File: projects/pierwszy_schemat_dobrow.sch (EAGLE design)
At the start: 36 parts, among them IC1 74HC595N, IC2 7805T, IC3 LD117AV, U2 ARDUINOR3-DIMENSION

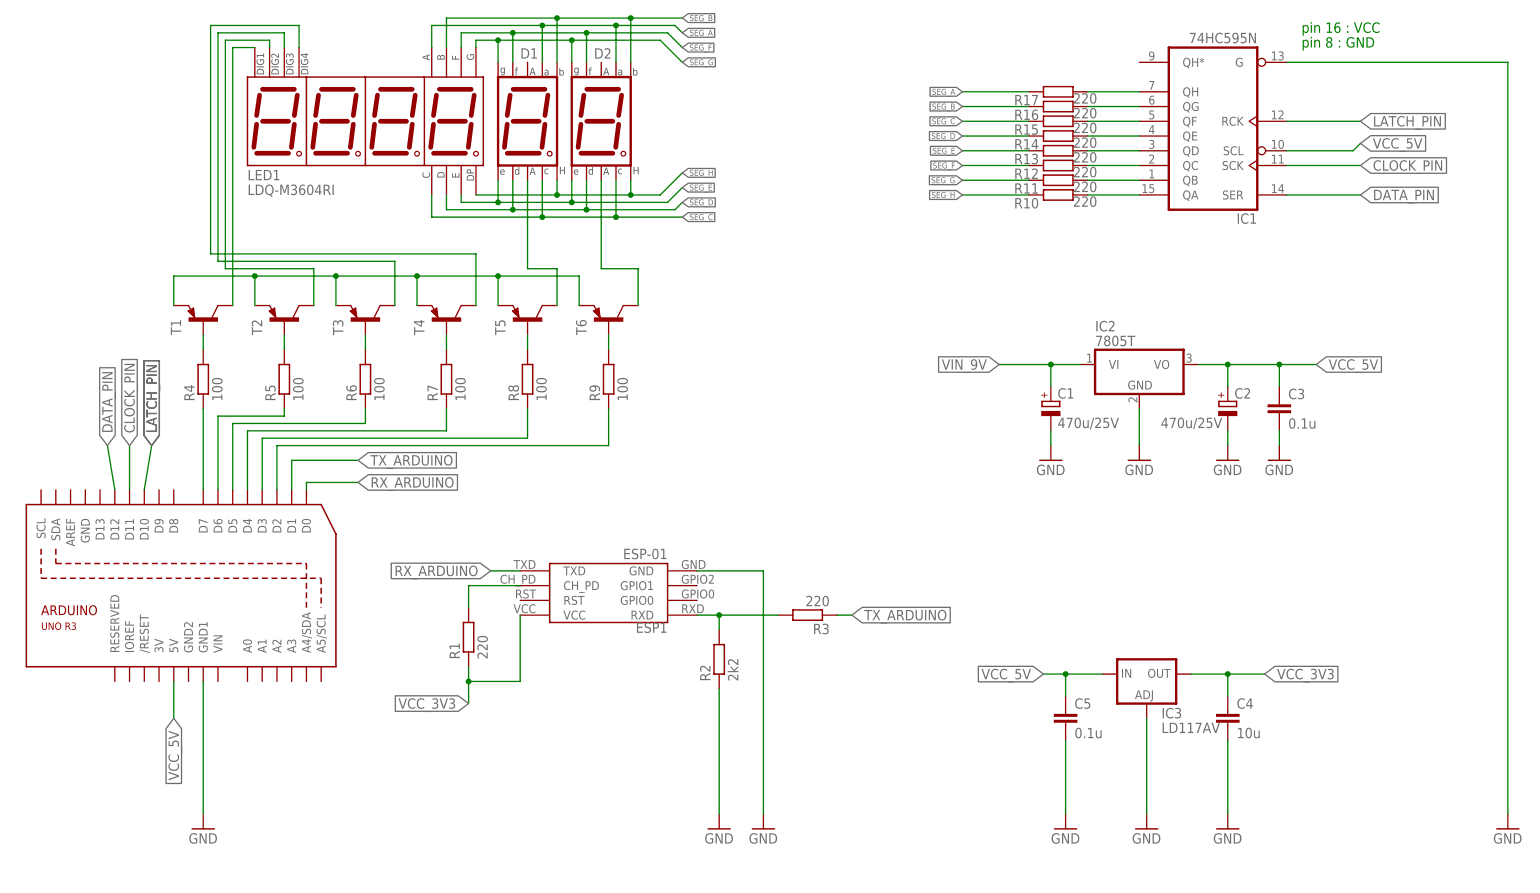
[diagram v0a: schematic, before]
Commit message: changed arduino to pro mini
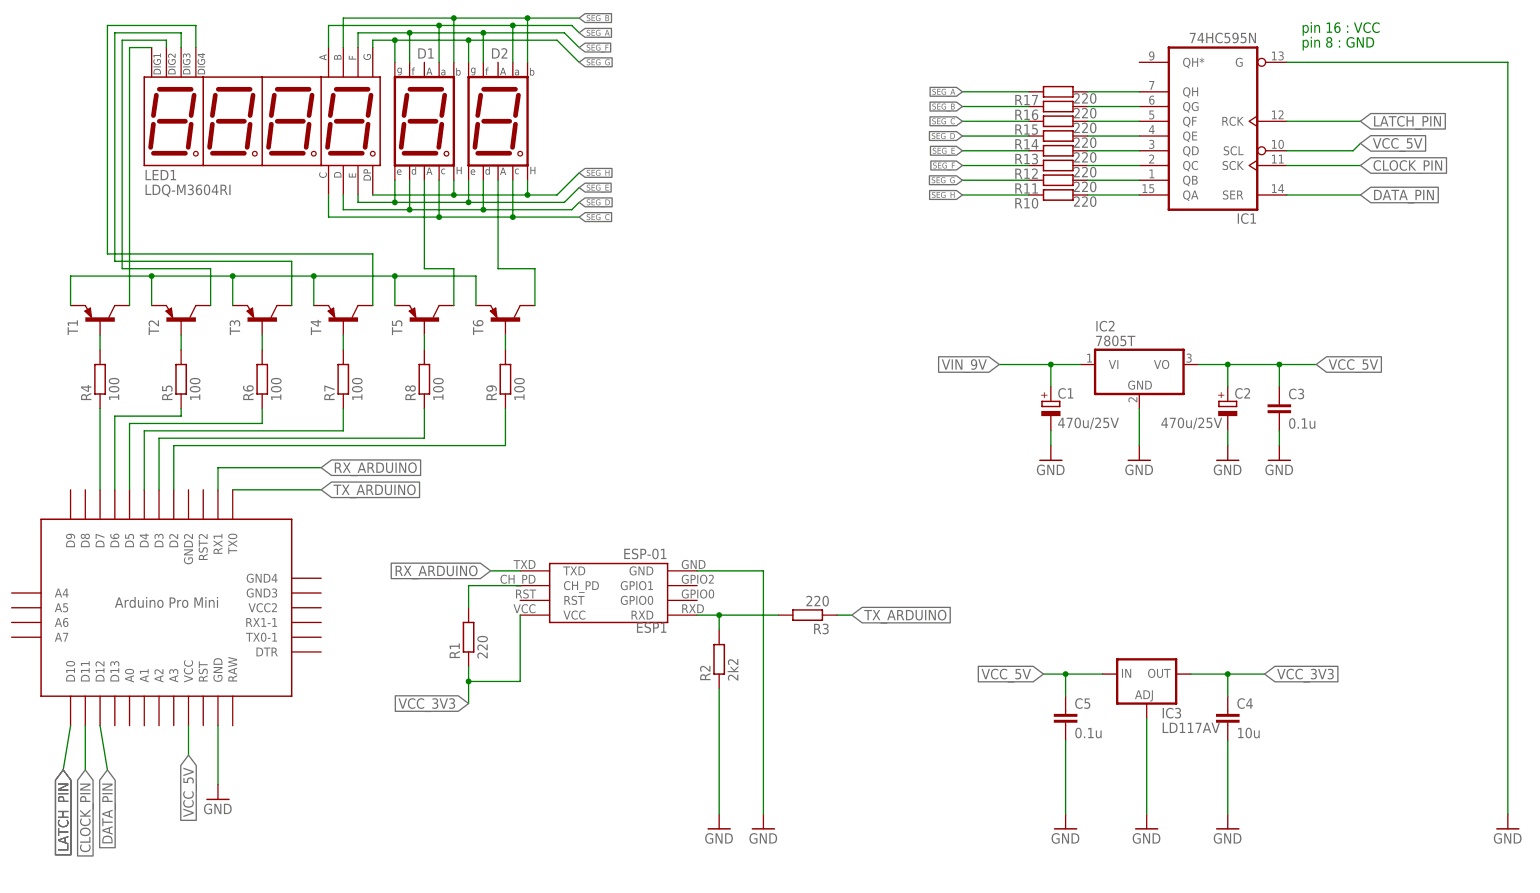
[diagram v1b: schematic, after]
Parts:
- removed U2: ARDUINOR3-DIMENSION, arduino_UNO_edit:ARDUINOR3-DIMENSION
- added U$1: PRO-MINI, Arduino-clone:PRO-MINI
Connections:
- removed net N$20: U2.GND1
- net CLOCK_PIN: now also U$1.D11; no longer U2.D11
- net DATA_PIN: now also U$1.D12; no longer U2.D12
- net GND: now also U$1.GND
- net LATCH_PIN: now also U$1.D10; no longer U2.D10
- net N$31: now also U$1.D7; no longer U2.D7
- net N$32: now also U$1.D6; no longer U2.D6
- net N$33: now also U$1.D5; no longer U2.D5
- net N$34: now also U$1.D4; no longer U2.D4
- net N$35: now also U$1.D3; no longer U2.D3
- net N$36: now also U$1.D2; no longer U2.D2
- net RX_ARDUINO: now also U$1.RX1; no longer U2.D0
- net TX_ARDUINO: now also U$1.TX0; no longer U2.D1
- net VCC_5V: now also U$1.VCC; no longer U2.5V
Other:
- moved on the sheet: D1, D2, LED1, R4, R5, R6, R7, R8, R9, T1, T2, T3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

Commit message: repaired gnd connection
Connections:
- removed net N$21: C2.-
- net GND: now also C2.-
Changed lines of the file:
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@@
 <setting verticaltext="up"/>
 </settings>
-<grid distance="1.27" unitdist="mm" unit="mm" style="lines" multiple="1" display="yes" altdistance="0.01" altunitdist="inch" altunit="inch"/>
+<grid distance="0.1" unitdist="inch" unit="inch" style="lines" multiple="1" display="no" altdistance="0.01" altunitdist="inch" altunit="inch"/>
 <layers>
 <layer number="1" name="Top" color="4" fill="1" visible="no" active="no"/>
@@
 <part name="C3" library="rcl" library_urn="urn:adsk.eagle:library:334" deviceset="C-EU" device="025-025X050" package3d_urn="urn:adsk.eagle:package:23629/2" value="0.1u"/>
 <part name="GND2" library="supply1" library_urn="urn:adsk.eagle:library:371" deviceset="GND" device=""/>
-<part name="GND6" library="supply1" library_urn="urn:adsk.eagle:library:371" deviceset="GND" device=""/>
 <part name="GND7" library="supply1" library_urn="urn:adsk.eagle:library:371" deviceset="GND" device=""/>
 <part name="IC3" library="v-reg" library_urn="urn:adsk.eagle:library:409" deviceset="LD117A?*" device="V" package3d_urn="urn:adsk.eagle:package:30365/1"/>
@@
 <part name="FRAME1" library="frames" library_urn="urn:adsk.eagle:library:229" deviceset="DOCFIELD" device=""/>
 <part name="U$1" library="Arduino-clone" deviceset="PRO-MINI" device=""/>
+<part name="GND6" library="supply1" library_urn="urn:adsk.eagle:library:371" deviceset="GND" device=""/>
 </parts>
 <sheets>
@@
 <attribute name="VALUE" x="185.42" y="106.68" size="1.778" layer="96"/>
 </instance>
-<instance part="GND6" gate="1" x="218.44" y="109.22" smashed="yes">
-<attribute name="VALUE" x="215.9" y="106.68" size="1.778" layer="96"/>
-</instance>
 <instance part="GND7" gate="1" x="227.33" y="109.22" smashed="yes">
 <attribute name="VALUE" x="224.79" y="106.68" size="1.778" layer="96"/>
@@
 </instance>
 <instance part="U$1" gate="G$1" x="26.67" y="81.28" smashed="yes" rot="R270"/>
+<instance part="GND6" gate="1" x="218.44" y="109.22" smashed="yes">
+<attribute name="VALUE" x="215.9" y="106.68" size="1.778" layer="96"/>
+</instance>
 </instances>
 <busses>
@@
 <wire x1="44.45" y1="53.34" x2="44.45" y2="63.5" width="0.1524" layer="91"/>
 </segment>
+<segment>
+<pinref part="C2" gate="G$1" pin="-"/>
+<wire x1="218.44" y1="114.3" x2="218.44" y2="111.76" width="0.1524" layer="91"/>
+<pinref part="GND6" gate="1" pin="GND"/>
+</segment>
 </net>
 <net name="TX_ARDUINO" class="0">
@@
 </segment>
 </net>
-<net name="N$21" class="0">
-<segment>
-<pinref part="C2" gate="G$1" pin="-"/>
-<wire x1="218.44" y1="114.3" x2="218.44" y2="111.76" width="0.1524" layer="91"/>
-<pinref part="GND6" gate="1" pin="GND"/>
-</segment>
-</net>

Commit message: repair v2
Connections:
- removed net N$11: C1.-
- net GND: now also C1.-
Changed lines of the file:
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@@
 <part name="C2" library="rcl" library_urn="urn:adsk.eagle:library:334" deviceset="CPOL-EU" device="E5-8.5" package3d_urn="urn:adsk.eagle:package:23374/1" value="470u/25V"/>
 <part name="C3" library="rcl" library_urn="urn:adsk.eagle:library:334" deviceset="C-EU" device="025-025X050" package3d_urn="urn:adsk.eagle:package:23629/2" value="0.1u"/>
-<part name="GND2" library="supply1" library_urn="urn:adsk.eagle:library:371" deviceset="GND" device=""/>
 <part name="GND7" library="supply1" library_urn="urn:adsk.eagle:library:371" deviceset="GND" device=""/>
 <part name="IC3" library="v-reg" library_urn="urn:adsk.eagle:library:409" deviceset="LD117A?*" device="V" package3d_urn="urn:adsk.eagle:package:30365/1"/>
@@
 <part name="U$1" library="Arduino-clone" deviceset="PRO-MINI" device=""/>
 <part name="GND6" library="supply1" library_urn="urn:adsk.eagle:library:371" deviceset="GND" device=""/>
+<part name="GND2" library="supply1" library_urn="urn:adsk.eagle:library:371" deviceset="GND" device=""/>
 </parts>
 <sheets>
@@
 <attribute name="VALUE" x="228.854" y="114.681" size="1.778" layer="96"/>
 </instance>
-<instance part="GND2" gate="1" x="187.96" y="109.22" smashed="yes">
-<attribute name="VALUE" x="185.42" y="106.68" size="1.778" layer="96"/>
-</instance>
 <instance part="GND7" gate="1" x="227.33" y="109.22" smashed="yes">
 <attribute name="VALUE" x="224.79" y="106.68" size="1.778" layer="96"/>
@@
 <instance part="GND6" gate="1" x="218.44" y="109.22" smashed="yes">
 <attribute name="VALUE" x="215.9" y="106.68" size="1.778" layer="96"/>
+</instance>
+<instance part="GND2" gate="1" x="187.96" y="109.22" smashed="yes">
+<attribute name="VALUE" x="185.42" y="106.68" size="1.778" layer="96"/>
 </instance>
 </instances>
@@
 <pinref part="GND6" gate="1" pin="GND"/>
 </segment>
+<segment>
+<pinref part="C1" gate="G$1" pin="-"/>
+<wire x1="187.96" y1="114.3" x2="187.96" y2="111.76" width="0.1524" layer="91"/>
+<pinref part="GND2" gate="1" pin="GND"/>
+</segment>
 </net>
 <net name="TX_ARDUINO" class="0">
@@
 </segment>
 </net>
-<net name="N$11" class="0">
-<segment>
-<pinref part="C1" gate="G$1" pin="-"/>
-<wire x1="187.96" y1="114.3" x2="187.96" y2="111.76" width="0.1524" layer="91"/>
-<pinref part="GND2" gate="1" pin="GND"/>
-</segment>
-</net>

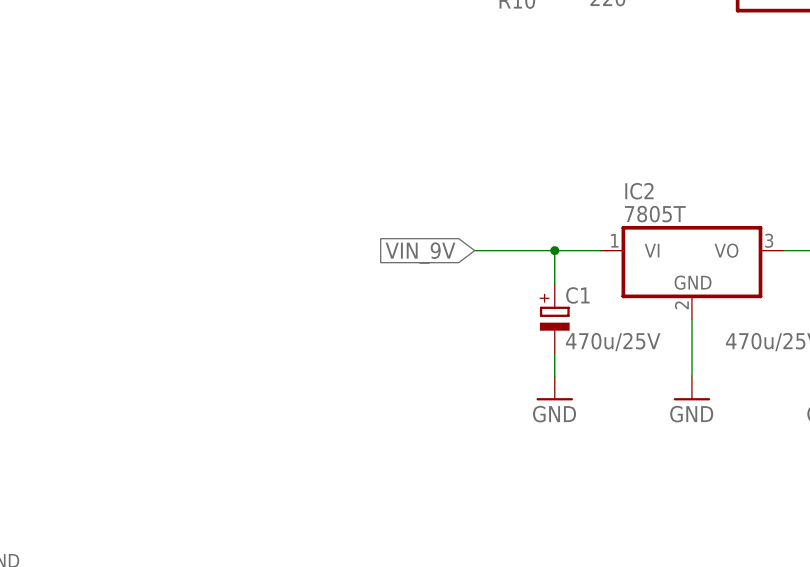
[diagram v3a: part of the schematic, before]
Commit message: Added power jack
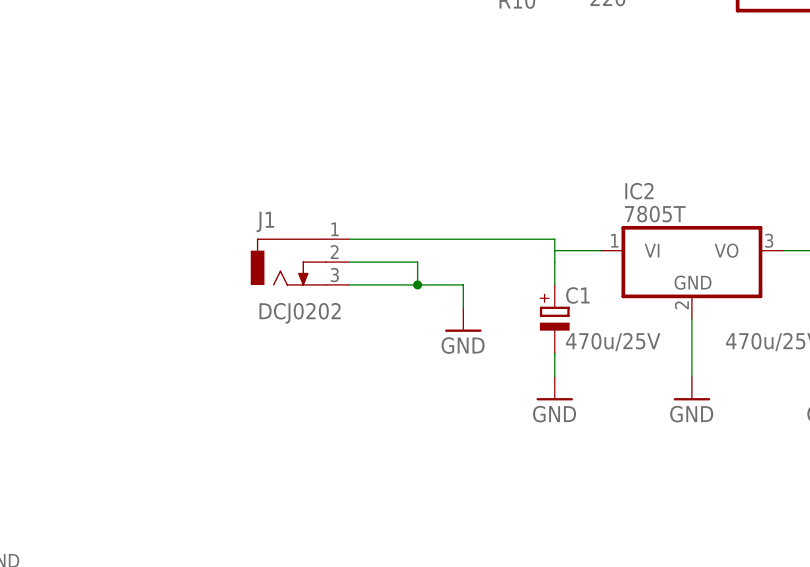
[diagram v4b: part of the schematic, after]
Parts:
- added J1: DCJ0202, con-jack:DCJ0202
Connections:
- net GND: now also J1.2, J1.3
- net VIN_9V: now also J1.1
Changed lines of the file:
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@@
 <layers>
 <layer number="1" name="Top" color="4" fill="1" visible="no" active="no"/>
+<layer number="2" name="Route2" color="1" fill="3" visible="no" active="no"/>
+<layer number="3" name="Route3" color="4" fill="3" visible="no" active="no"/>
+<layer number="4" name="Route4" color="1" fill="4" visible="no" active="no"/>
+<layer number="5" name="Route5" color="4" fill="4" visible="no" active="no"/>
+<layer number="6" name="Route6" color="1" fill="8" visible="no" active="no"/>
+<layer number="7" name="Route7" color="4" fill="8" visible="no" active="no"/>
+<layer number="8" name="Route8" color="1" fill="2" visible="no" active="no"/>
+<layer number="9" name="Route9" color="4" fill="2" visible="no" active="no"/>
+<layer number="10" name="Route10" color="1" fill="7" visible="no" active="no"/>
+<layer number="11" name="Route11" color="4" fill="7" visible="no" active="no"/>
+<layer number="12" name="Route12" color="1" fill="5" visible="no" active="no"/>
+<layer number="13" name="Route13" color="4" fill="5" visible="no" active="no"/>
+<layer number="14" name="Route14" color="1" fill="6" visible="no" active="no"/>
+<layer number="15" name="Route15" color="4" fill="6" visible="no" active="no"/>
 <layer number="16" name="Bottom" color="1" fill="1" visible="no" active="no"/>
 <layer number="17" name="Pads" color="2" fill="1" visible="no" active="no"/>
@@
 <part name="GND6" library="supply1" library_urn="urn:adsk.eagle:library:371" deviceset="GND" device=""/>
 <part name="GND2" library="supply1" library_urn="urn:adsk.eagle:library:371" deviceset="GND" device=""/>
+<part name="J1" library="con-jack" library_urn="urn:adsk.eagle:library:154" deviceset="DCJ0202" device="" package3d_urn="urn:adsk.eagle:package:7491/1"/>
+<part name="GND12" library="supply1" library_urn="urn:adsk.eagle:library:371" deviceset="GND" device=""/>
 </parts>
 <sheets>
@@
 <instance part="GND2" gate="1" x="187.96" y="109.22" smashed="yes">
 <attribute name="VALUE" x="185.42" y="106.68" size="1.778" layer="96"/>
+</instance>
+<instance part="J1" gate="G$1" x="157.48" y="124.46" smashed="yes">
+<attribute name="NAME" x="154.94" y="128.27" size="1.778" layer="95"/>
+<attribute name="VALUE" x="154.94" y="118.11" size="1.778" layer="96"/>
+</instance>
+<instance part="GND12" gate="1" x="177.8" y="116.84" smashed="yes">
+<attribute name="VALUE" x="175.26" y="114.3" size="1.778" layer="96"/>
 </instance>
 </instances>
@@
 <pinref part="GND2" gate="1" pin="GND"/>
 </segment>
+<segment>
+<pinref part="J1" gate="G$1" pin="3"/>
+<pinref part="GND12" gate="1" pin="GND"/>
+<wire x1="165.1" y1="121.92" x2="172.72" y2="121.92" width="0.1524" layer="91"/>
+<wire x1="172.72" y1="121.92" x2="177.8" y2="121.92" width="0.1524" layer="91"/>
+<wire x1="177.8" y1="121.92" x2="177.8" y2="119.38" width="0.1524" layer="91"/>
+<pinref part="J1" gate="G$1" pin="2"/>
+<wire x1="165.1" y1="124.46" x2="172.72" y2="124.46" width="0.1524" layer="91"/>
+<wire x1="172.72" y1="124.46" x2="172.72" y2="121.92" width="0.1524" layer="91"/>
+<junction x="172.72" y="121.92"/>
+</segment>
 </net>
 <net name="TX_ARDUINO" class="0">
@@
 <wire x1="193.04" y1="125.73" x2="187.96" y2="125.73" width="0.1524" layer="91"/>
 <pinref part="C1" gate="G$1" pin="+"/>
-<wire x1="187.96" y1="125.73" x2="179.07" y2="125.73" width="0.1524" layer="91"/>
-<wire x1="187.96" y1="121.92" x2="187.96" y2="125.73" width="0.1524" layer="91"/>
-<junction x="187.96" y="125.73"/>
-<label x="179.07" y="125.73" size="1.778" layer="95" rot="R180" xref="yes"/>
-</segment>
-</net>
+<wire x1="187.96" y1="121.92" x2="187.96" y2="124.46" width="0.1524" layer="91"/>
+<pinref part="J1" gate="G$1" pin="1"/>
+<wire x1="187.96" y1="124.46" x2="187.96" y2="125.73" width="0.1524" layer="91"/>
+<wire x1="165.1" y1="127" x2="187.96" y2="127" width="0.1524" layer="91"/>
+<wire x1="187.96" y1="127" x2="187.96" y2="125.73" width="0.1524" layer="91"/>
+</segment>
+</net>
